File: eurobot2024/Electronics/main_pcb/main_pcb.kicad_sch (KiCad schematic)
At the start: 58 parts, among them J1 PI40HAT, J10 Conn_01x02_Male, J11 Conn_01x03_Male, J12 Conn_01x02_Male, J13 Conn_01x02_Male, J15 Conn_01x02_Male, J16 Conn_01x02_Male, J17 Conn_01x03_Male, J18 Conn_01x03_Male, J2 Conn_01x02_Male, J2 Conn_01x04_Male, J20 Conn_01x05, J21 Conn_01x05, J22 Conn_01x05, J23 22-03-5035, J24 Conn_01x02_Male, J3 Conn_01x02_Male, J4 Conn_01x02_Male, J5 Conn_01x02_Male, J6 Conn_01x02_Male, J8 Conn_01x02_Male, J9 22-03-5035, P1 R-78Bxx-2.0, P2 Amazon 10A stepdown, Q1 NVTR4503NT1G, Q2 NVTR4503NT1G, Q3 NVTR4503NT1G, Q7 NVTR4503NT1G, U1 74LVC1G125, U2 SN74LVC1G04DRLR, U3 PCA9306D, U4 Pololu_MAX14870, U5 PCA9685PW, U6 Pololu_MAX14870, U7 SN74AHCT1G126

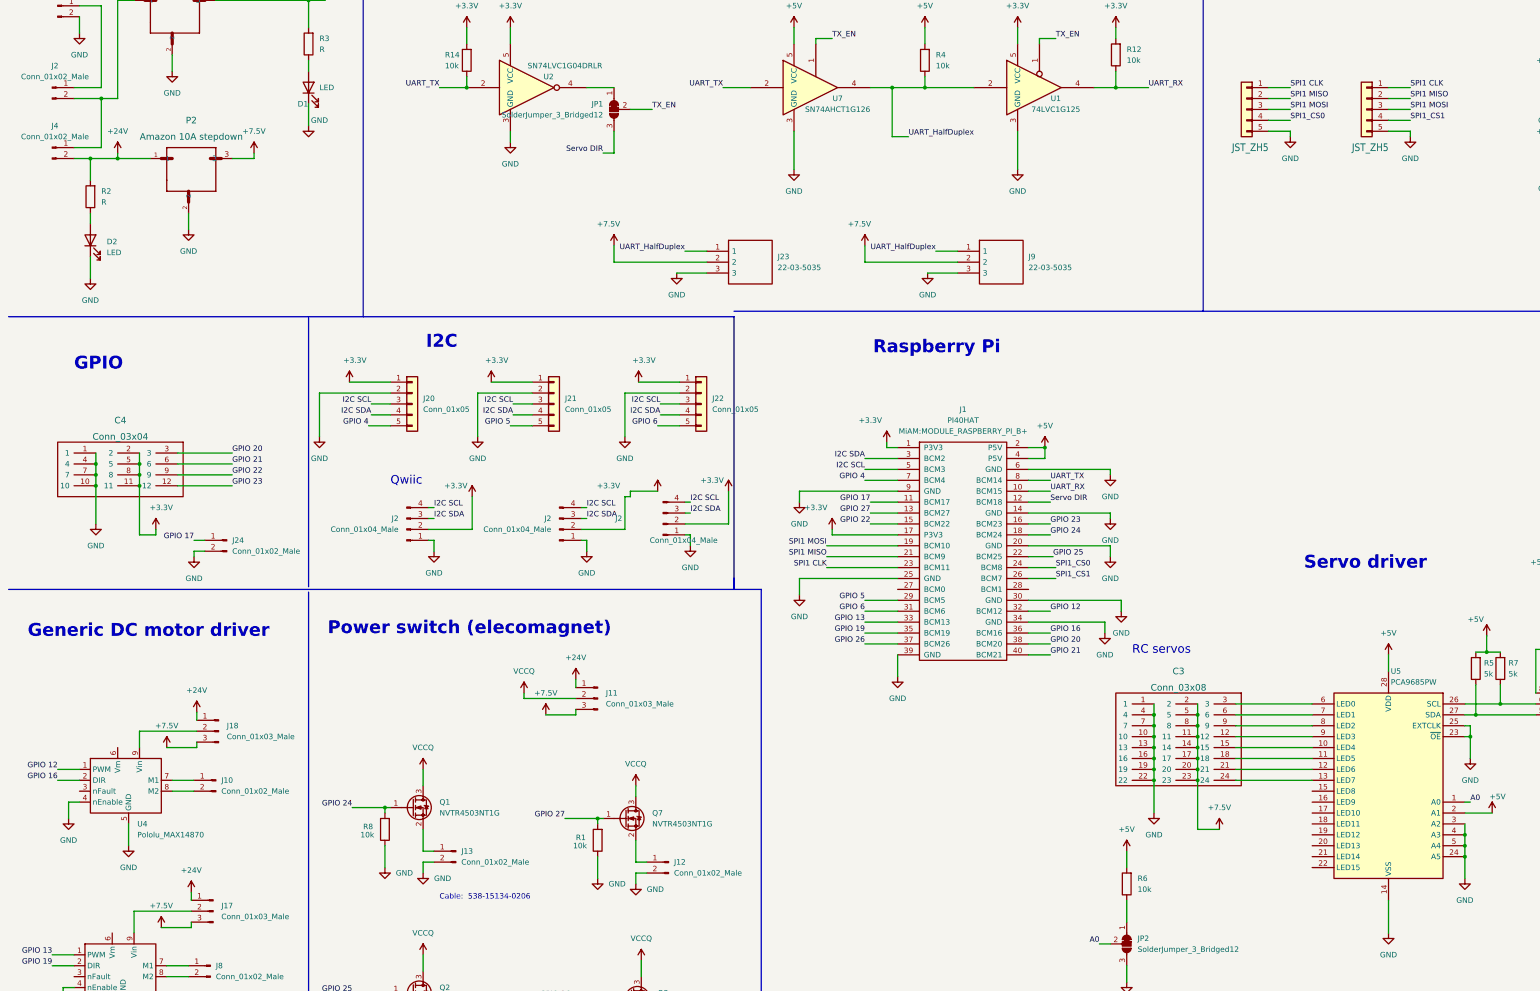
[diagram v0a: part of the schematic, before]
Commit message: Rename SPI1 to SPI0 & add some text
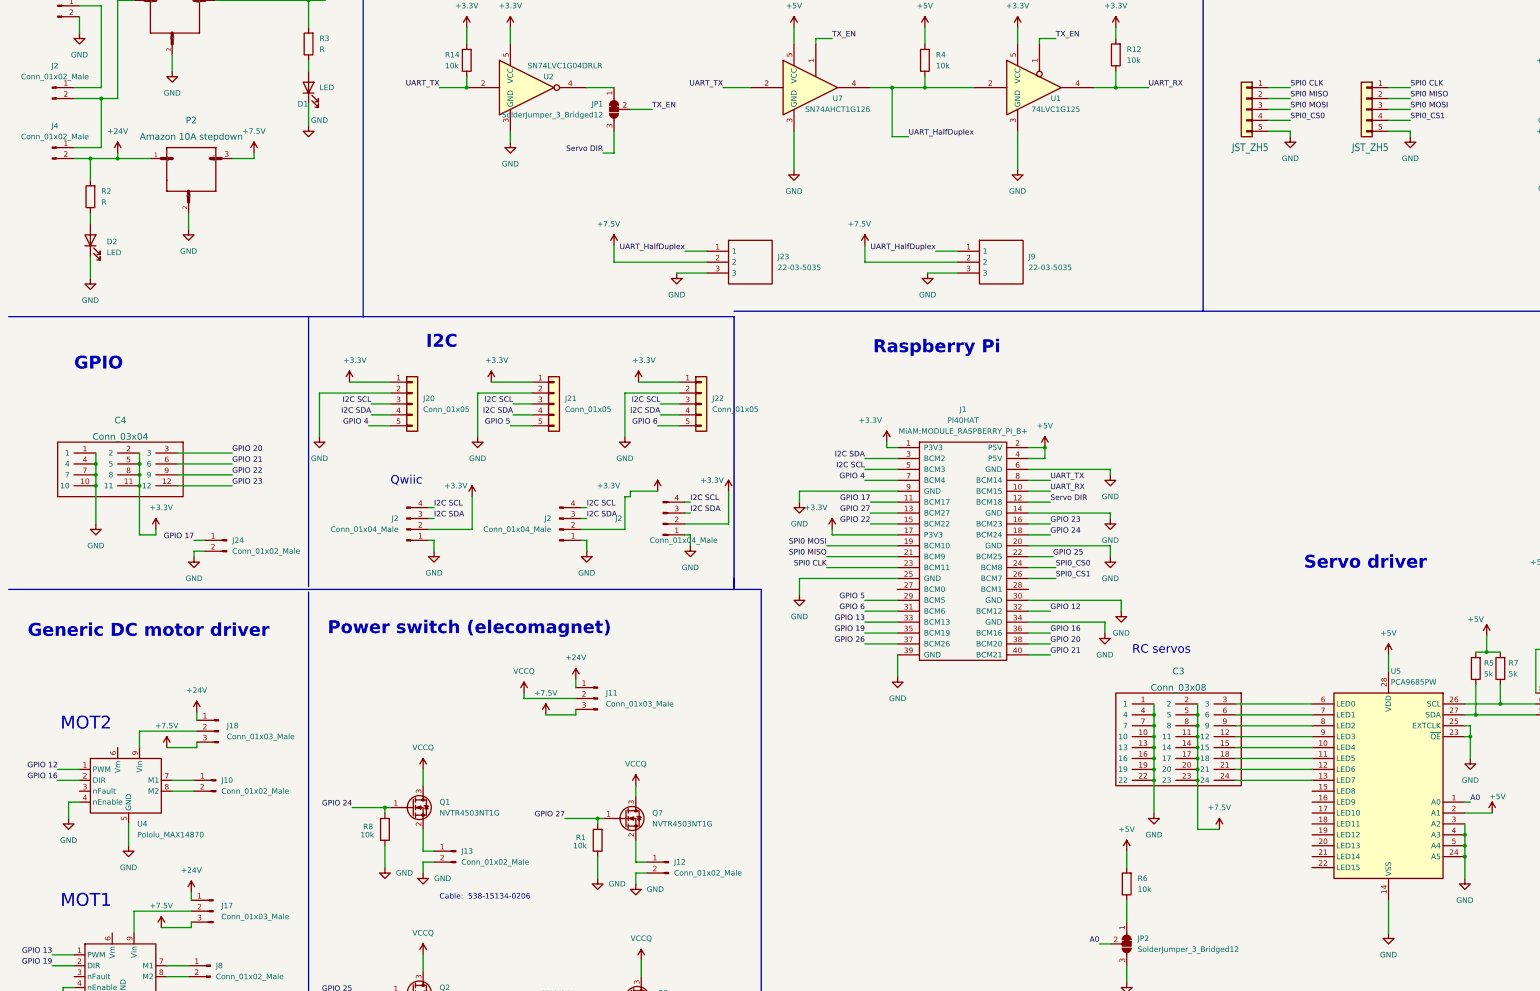
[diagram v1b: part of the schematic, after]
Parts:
- renumbered SPI1 to SPI0
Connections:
- net SPI1 CLK renamed SPI0 CLK
- net SPI1 MISO renamed SPI0 MISO
- net SPI1 MOSI renamed SPI0 MOSI
- net SPI1_CS0 renamed SPI0_CS0
- net SPI1_CS1 renamed SPI0_CS1
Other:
- note added: "MOT1"
- note added: "MOT2"
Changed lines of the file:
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@@
     (effects (font (size 3 3) (thickness 0.8) bold) (justify left bottom))
   )
+  (text "MOT1\n" (at 24.765 239.395 0)
+    (effects (font (size 3 3)) (justify left bottom))
+  )
   (text "Smart Servos - 3.3V to 5V UART half-duplex" (at 100.33 20.32 0)
     (effects (font (size 3 3) (thickness 0.8) bold) (justify left bottom))
@@
     (effects (font (size 1.27 1.27)) (justify left bottom))
   )
+  (text "MOT2" (at 24.765 198.12 0)
+    (effects (font (size 3 3)) (justify left bottom))
+  )
   (text "Raspberry Pi" (at 213.995 110.49 0)
     (effects (font (size 3 3) (thickness 0.8) bold) (justify left bottom))
@@
     (effects (font (size 1.27 1.27)) (justify right bottom))
   )
-  (label "SPI1 CLK" (at 311.15 48.26 0) (fields_autoplaced)
+  (label "SPI0 CLK" (at 311.15 48.26 0) (fields_autoplaced)
     (effects (font (size 1.27 1.27)) (justify left bottom))
   )
@@
     (effects (font (size 1.27 1.27)) (justify right bottom))
   )
-  (label "SPI1 MISO" (at 339.09 50.8 0) (fields_autoplaced)
+  (label "SPI0 MISO" (at 339.09 50.8 0) (fields_autoplaced)
     (effects (font (size 1.27 1.27)) (justify left bottom))
   )
@@
     (effects (font (size 1.27 1.27)) (justify left bottom))
   )
-  (label "SPI1 CLK" (at 203.2 160.02 180) (fields_autoplaced)
+  (label "SPI0 CLK" (at 203.2 160.02 180) (fields_autoplaced)
     (effects (font (size 1.27 1.27)) (justify right bottom))
   )
@@
     (effects (font (size 1.27 1.27)) (justify right bottom))
   )
-  (label "SPI1 MOSI" (at 203.2 154.94 180) (fields_autoplaced)
+  (label "SPI0 MOSI" (at 203.2 154.94 180) (fields_autoplaced)
     (effects (font (size 1.27 1.27)) (justify right bottom))
   )
@@
     (effects (font (size 1.27 1.27)) (justify left bottom))
   )
-  (label "SPI1_CS1" (at 339.09 55.88 0) (fields_autoplaced)
+  (label "SPI0_CS1" (at 339.09 55.88 0) (fields_autoplaced)
     (effects (font (size 1.27 1.27)) (justify left bottom))
   )
-  (label "SPI1 CLK" (at 339.09 48.26 0) (fields_autoplaced)
+  (label "SPI0 CLK" (at 339.09 48.26 0) (fields_autoplaced)
     (effects (font (size 1.27 1.27)) (justify left bottom))
   )
@@
     (effects (font (size 1.27 1.27)) (justify right bottom))
   )
-  (label "SPI1 MOSI" (at 311.15 53.34 0) (fields_autoplaced)
+  (label "SPI0 MOSI" (at 311.15 53.34 0) (fields_autoplaced)
     (effects (font (size 1.27 1.27)) (justify left bottom))
   )
@@
     (effects (font (size 1.27 1.27)) (justify right bottom))
   )
-  (label "SPI1 MOSI" (at 339.09 53.34 0) (fields_autoplaced)
+  (label "SPI0 MOSI" (at 339.09 53.34 0) (fields_autoplaced)
     (effects (font (size 1.27 1.27)) (justify left bottom))
   )
@@
     (effects (font (size 1.27 1.27)) (justify left bottom))
   )
-  (label "SPI1_CS1" (at 256.54 162.56 0) (fields_autoplaced)
+  (label "SPI0_CS1" (at 256.54 162.56 0) (fields_autoplaced)
     (effects (font (size 1.27 1.27)) (justify left bottom))
   )
@@
     (effects (font (size 1.27 1.27)) (justify right bottom))
   )
-  (label "SPI1_CS0" (at 256.54 160.02 0) (fields_autoplaced)
+  (label "SPI0_CS0" (at 256.54 160.02 0) (fields_autoplaced)
     (effects (font (size 1.27 1.27)) (justify left bottom))
   )
@@
     (effects (font (size 1.27 1.27)) (justify left bottom))
   )
-  (label "SPI1_CS0" (at 311.15 55.88 0) (fields_autoplaced)
+  (label "SPI0_CS0" (at 311.15 55.88 0) (fields_autoplaced)
     (effects (font (size 1.27 1.27)) (justify left bottom))
   )
@@
     (effects (font (size 1.27 1.27)) (justify right bottom))
   )
-  (label "SPI1 MISO" (at 203.2 157.48 180) (fields_autoplaced)
+  (label "SPI0 MISO" (at 203.2 157.48 180) (fields_autoplaced)
     (effects (font (size 1.27 1.27)) (justify right bottom))
   )
@@
     (effects (font (size 1.27 1.27)) (justify left bottom))
   )
-  (label "SPI1 MISO" (at 311.15 50.8 0) (fields_autoplaced)
+  (label "SPI0 MISO" (at 311.15 50.8 0) (fields_autoplaced)
     (effects (font (size 1.27 1.27)) (justify left bottom))
   )
@@
   (symbol (lib_id "Connector_Generic:Conn_01x05") (at 300.99 53.34 0) (mirror y) (unit 1)
     (in_bom yes) (on_board yes) (dnp no)
-    (property "Reference" "SPI1" (at 306.07 44.958 0)
+    (property "Reference" "SPI0" (at 306.07 44.958 0)
       (effects (font (size 1.778 1.5113)) (justify left bottom) hide)
     )
@@
       (project "nautilus"
         (path "/153372ee-bcdd-4b24-a68f-0b89c1a33ebf"
-          (reference "SPI1") (unit 1)
+          (reference "SPI0") (unit 1)
         )
       )
       (project "main_pcb"
         (path "/b6ea65bf-12e3-449e-a49e-1f1611fcebc1"
-          (reference "SPI1") (unit 1)
+          (reference "SPI0") (unit 1)
         )
       )
@@
   (symbol (lib_id "Connector_Generic:Conn_01x05") (at 328.93 53.34 0) (mirror y) (unit 1)
     (in_bom yes) (on_board yes) (dnp no)
-    (property "Reference" "SPI1" (at 334.01 44.958 0)
+    (property "Reference" "SPI0" (at 334.01 44.958 0)
       (effects (font (size 1.778 1.5113)) (justify left bottom) hide)
     )
@@
       (project "nautilus"
         (path "/153372ee-bcdd-4b24-a68f-0b89c1a33ebf"
-          (reference "SPI1") (unit 1)
+          (reference "SPI0") (unit 1)
         )
       )

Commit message: Main robot PCB order
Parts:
- J13: Mouser Part Number (none) -> 538-53047-0210; RS 538-53047-0210 -> (none)
- U1: Mouser 595-SN74LVC1G125DRLR -> (none); Mouser Part Number (none) -> 595-SN74LVC1G125DRLR
- U2: Mouser 595-SN74LVC1G04DRLR -> (none); Mouser Part Number (none) -> 595-SN74LVC1G04DRLR
- U7: Mouser 595-SNAHCT1G126DBVR -> (none); Mouser Part Number (none) -> 595-SNAHCT1G126DBVR
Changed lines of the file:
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@@
       (effects (font (size 1.27 1.27)) hide)
     )
-    (property "Mouser" " 595-SNAHCT1G126DBVR " (at 200.66 48.26 0)
+    (property "Mouser Part Number" " 595-SNAHCT1G126DBVR " (at 200.66 48.26 0)
       (effects (font (size 1.27 1.27)) hide)
     )
@@
       (effects (font (size 1.27 1.27)) hide)
     )
-    (property "Mouser" " 595-SN74LVC1G04DRLR " (at 134.62 48.26 0)
+    (property "Mouser Part Number" " 595-SN74LVC1G04DRLR " (at 134.62 48.26 0)
       (effects (font (size 1.27 1.27)) hide)
     )
@@
       (effects (font (size 1.27 1.27)) hide)
     )
-    (property "Mouser" " 595-SN74LVC1G125DRLR " (at 252.73 48.26 0)
+    (property "Mouser Part Number" " 595-SN74LVC1G125DRLR " (at 252.73 48.26 0)
       (effects (font (size 1.27 1.27)) hide)
     )
@@
       (effects (font (size 1.27 1.27)) hide)
     )
-    (property "RS" " 538-53047-0210 " (at 116.84 226.06 0)
+    (property "Mouser Part Number" " 538-53047-0210 " (at 116.84 226.06 0)
       (effects (font (size 1.27 1.27)) hide)
     )

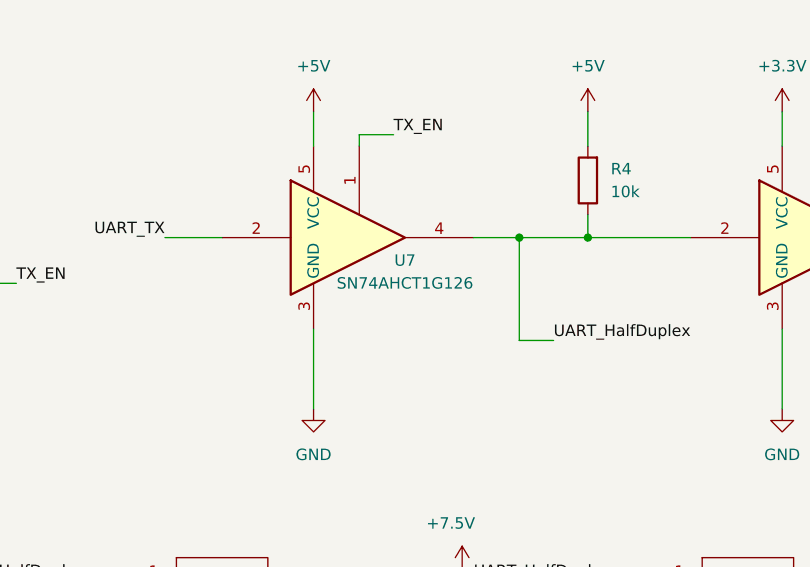
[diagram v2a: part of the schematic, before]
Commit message: Implement fully action-based strategy framework for 2024 robot.
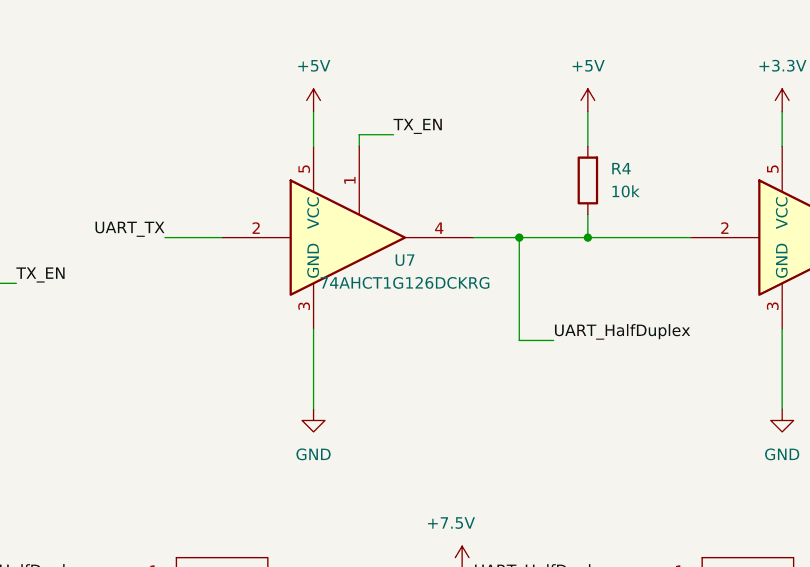
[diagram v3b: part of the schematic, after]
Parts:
- U3: footprint Package_SO:SOP-8_3.76x4.96mm_P1.27mm -> Package_SO:SSOP-8_2.95x2.8mm_P0.65mm
- U7: value SN74AHCT1G126 -> 74AHCT1G126DCKRG; Mouser Part Number 595-SNAHCT1G126DBVR -> 595-74AHCT1G126DCKRG
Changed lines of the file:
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@@
       (effects (font (size 1.27 1.27)))
     )
-    (property "Value" "SN74AHCT1G126" (at 205.74 53.34 0)
+    (property "Value" "74AHCT1G126DCKRG " (at 205.74 53.34 0)
       (effects (font (size 1.27 1.27)))
     )
@@
       (effects (font (size 1.27 1.27)) hide)
     )
-    (property "Mouser Part Number" " 595-SNAHCT1G126DBVR " (at 200.66 48.26 0)
+    (property "Mouser Part Number" " 595-74AHCT1G126DCKRG " (at 200.66 48.26 0)
       (effects (font (size 1.27 1.27)) hide)
     )
@@
       (effects (font (size 1.27 1.27)) (justify right))
     )
-    (property "Footprint" "Package_SO:SOP-8_3.76x4.96mm_P1.27mm" (at 378.46 203.2 0)
-      (effects (font (size 1.27 1.27)) hide)
-    )
+    (property "Footprint" "Package_SO:SSOP-8_2.95x2.8mm_P0.65mm" (at 378.46 203.2 0)
+      (effects (font (size 1.27 1.27)) hide)
+    )

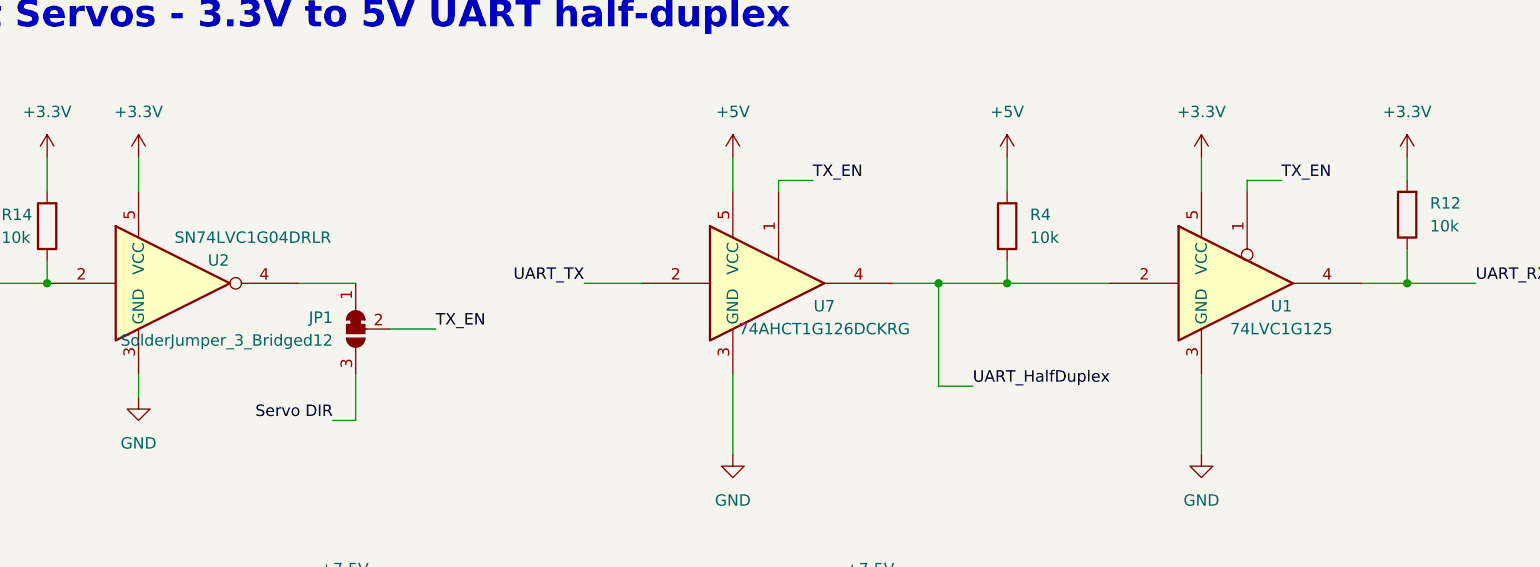
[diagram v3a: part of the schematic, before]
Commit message: [main_pcb] Update component footprint for easier soldering
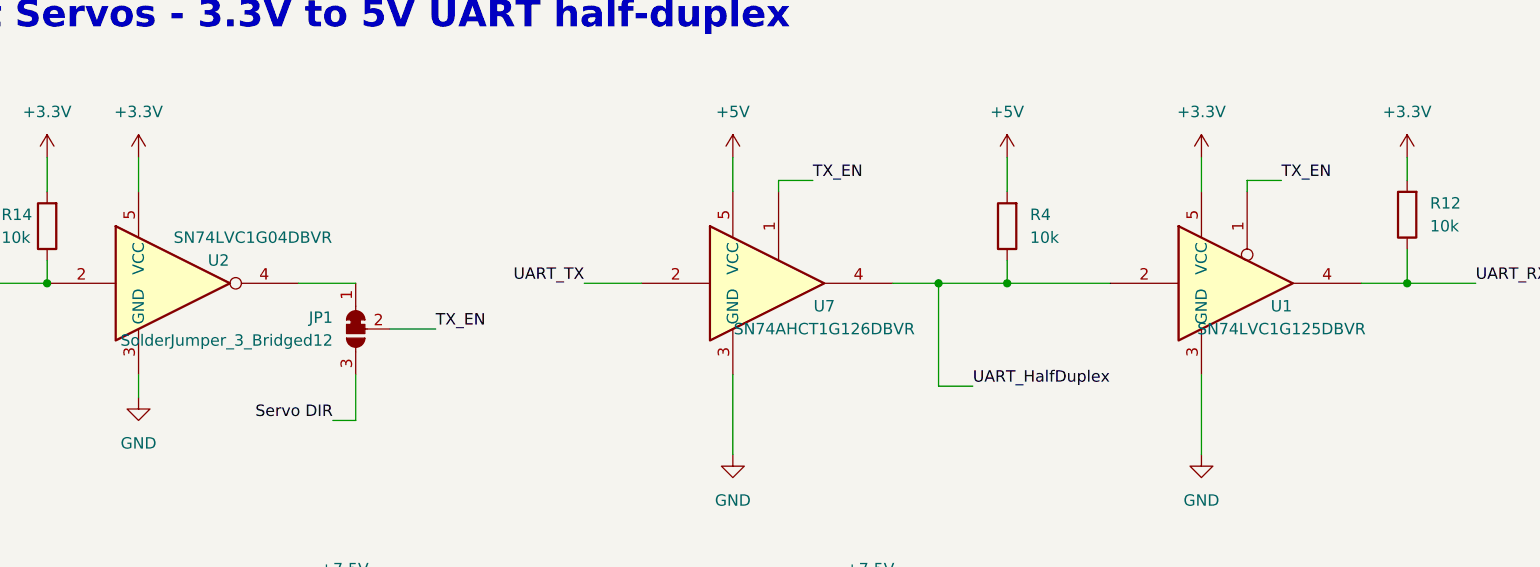
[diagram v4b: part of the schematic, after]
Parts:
- U1: value 74LVC1G125 -> SN74LVC1G125DBVR; footprint Package_TO_SOT_SMD:SOT-553 -> Package_TO_SOT_SMD:SOT-23-5_HandSoldering; Mouser Part Number 595-SN74LVC1G125DRLR -> 595-SN74LVC1G125DBVR
- U2: value SN74LVC1G04DRLR -> SN74LVC1G04DBVR; footprint Package_TO_SOT_SMD:SOT-553 -> Package_TO_SOT_SMD:SOT-23-5_HandSoldering; Mouser Part Number 595-SN74LVC1G04DRLR -> 595-SN74LVC1G04DBVR
- U7: value 74AHCT1G126DCKRG -> SN74AHCT1G126DBVR; footprint Package_TO_SOT_SMD:SOT-553 -> Package_TO_SOT_SMD:SOT-23-5_HandSoldering; Mouser Part Number 595-74AHCT1G126DCKRG -> 595-SNAHCT1G126DBVR
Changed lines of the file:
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@@
       (effects (font (size 1.27 1.27)))
     )
-    (property "Value" "74AHCT1G126DCKRG " (at 205.74 53.34 0)
+    (property "Value" "SN74AHCT1G126DBVR " (at 205.74 53.34 0)
       (effects (font (size 1.27 1.27)))
     )
-    (property "Footprint" "Package_TO_SOT_SMD:SOT-553" (at 200.66 48.26 0)
+    (property "Footprint" "Package_TO_SOT_SMD:SOT-23-5_HandSoldering" (at 200.66 48.26 0)
       (effects (font (size 1.27 1.27)) hide)
     )
@@
       (effects (font (size 1.27 1.27)) hide)
     )
-    (property "Mouser Part Number" " 595-74AHCT1G126DCKRG " (at 200.66 48.26 0)
+    (property "Mouser Part Number" " 595-SNAHCT1G126DBVR " (at 200.66 48.26 0)
       (effects (font (size 1.27 1.27)) hide)
     )
@@
       (effects (font (size 1.27 1.27)))
     )
-    (property "Value" "SN74LVC1G04DRLR " (at 142.24 43.18 0)
+    (property "Value" "SN74LVC1G04DBVR " (at 142.24 43.18 0)
       (effects (font (size 1.27 1.27)))
     )
-    (property "Footprint" "Package_TO_SOT_SMD:SOT-553" (at 134.62 48.26 0)
+    (property "Footprint" "Package_TO_SOT_SMD:SOT-23-5_HandSoldering" (at 134.62 48.26 0)
       (effects (font (size 1.27 1.27)) hide)
     )
@@
       (effects (font (size 1.27 1.27)) hide)
     )
-    (property "Mouser Part Number" " 595-SN74LVC1G04DRLR " (at 134.62 48.26 0)
+    (property "Mouser Part Number" " 595-SN74LVC1G04DBVR " (at 134.62 48.26 0)
       (effects (font (size 1.27 1.27)) hide)
     )
@@
       (effects (font (size 1.27 1.27)))
     )
-    (property "Value" "74LVC1G125" (at 256.54 53.34 0)
+    (property "Value" "SN74LVC1G125DBVR " (at 256.54 53.34 0)
       (effects (font (size 1.27 1.27)))
     )
-    (property "Footprint" "Package_TO_SOT_SMD:SOT-553" (at 252.73 48.26 0)
+    (property "Footprint" "Package_TO_SOT_SMD:SOT-23-5_HandSoldering" (at 252.73 48.26 0)
       (effects (font (size 1.27 1.27)) hide)
     )
@@
       (effects (font (size 1.27 1.27)) hide)
     )
-    (property "Mouser Part Number" " 595-SN74LVC1G125DRLR " (at 252.73 48.26 0)
+    (property "Mouser Part Number" " 595-SN74LVC1G125DBVR " (at 252.73 48.26 0)
       (effects (font (size 1.27 1.27)) hide)
     )
